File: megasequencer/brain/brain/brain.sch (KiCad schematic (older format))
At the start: 6 parts

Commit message: Add more jacks to the schema
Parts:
- added D1, D2, D? (x2): D_Schottky, symbol Device:D_Schottky
- added D3, D5: D, symbol Device:D
- added J2: EXT_CLOCK_IN, Connector_Audio:Jack_3.5mm_QingPu_WQP-PJ398SM_Vertical_CircularHoles, symbol Connector:AudioJack2_SwitchT
- added J4: ZERO_IN, Connector_Audio:Jack_3.5mm_QingPu_WQP-PJ398SM_Vertical_CircularHoles, symbol Connector:AudioJack2_SwitchT
- added J5: EXT_RATE_CV, Connector_Audio:Jack_3.5mm_QingPu_WQP-PJ398SM_Vertical_CircularHoles, symbol Connector:AudioJack2_SwitchT
- added J?: EXT_POS_CV, Connector_Audio:Jack_3.5mm_QingPu_WQP-PJ398SM_Vertical_CircularHoles, symbol Connector:AudioJack2_SwitchT
- added J?: DIR_IN, Connector_Audio:Jack_3.5mm_QingPu_WQP-PJ398SM_Vertical_CircularHoles, symbol Connector:AudioJack2_SwitchT
- added R1, R?: 1K, Resistor_THT:R_Axial_DIN0207_L6.3mm_D2.5mm_P7.62mm_Horizontal, symbol Device:R
- added R2, R3, R4, R5, R6, R? (x5): 100K, Resistor_THT:R_Axial_DIN0207_L6.3mm_D2.5mm_P7.62mm_Horizontal, symbol Device:R
- added R7, R9, R? (x2): 10K, Resistor_THT:R_Axial_DIN0207_L6.3mm_D2.5mm_P7.62mm_Horizontal, symbol Device:R
- added R?: 91K, Resistor_THT:R_Axial_DIN0207_L6.3mm_D2.5mm_P7.62mm_Horizontal, symbol Device:R
- added R?: 51K, Resistor_THT:R_Axial_DIN0207_L6.3mm_D2.5mm_P7.62mm_Horizontal, symbol Device:R
- added R?: 36K, Resistor_THT:R_Axial_DIN0207_L6.3mm_D2.5mm_P7.62mm_Horizontal, symbol Device:R
- added R?: 27K, Resistor_THT:R_Axial_DIN0207_L6.3mm_D2.5mm_P7.62mm_Horizontal, symbol Device:R
- added R?: 20K, Resistor_THT:R_Axial_DIN0207_L6.3mm_D2.5mm_P7.62mm_Horizontal, symbol Device:R
- added R?: 15K, Resistor_THT:R_Axial_DIN0207_L6.3mm_D2.5mm_P7.62mm_Horizontal, symbol Device:R
- added R?: 12K, Resistor_THT:R_Axial_DIN0207_L6.3mm_D2.5mm_P7.62mm_Horizontal, symbol Device:R
- added R?: 9K1, Resistor_THT:R_Axial_DIN0207_L6.3mm_D2.5mm_P7.62mm_Horizontal, symbol Device:R
- added R?: 7K5, Resistor_THT:R_Axial_DIN0207_L6.3mm_D2.5mm_P7.62mm_Horizontal, symbol Device:R
- added R?: 5K6, Resistor_THT:R_Axial_DIN0207_L6.3mm_D2.5mm_P7.62mm_Horizontal, symbol Device:R
- added R?: 4K3, Resistor_THT:R_Axial_DIN0207_L6.3mm_D2.5mm_P7.62mm_Horizontal, symbol Device:R
- added R?: 3K1, Resistor_THT:R_Axial_DIN0207_L6.3mm_D2.5mm_P7.62mm_Horizontal, symbol Device:R
- added R?: 2K2, Resistor_THT:R_Axial_DIN0207_L6.3mm_D2.5mm_P7.62mm_Horizontal, symbol Device:R
- added R?: 1K5, Resistor_THT:R_Axial_DIN0207_L6.3mm_D2.5mm_P7.62mm_Horizontal, symbol Device:R
- added R?: 620, Resistor_THT:R_Axial_DIN0207_L6.3mm_D2.5mm_P7.62mm_Horizontal, symbol Device:R
- added RV1: RATE_IN_OFFSET, symbol Device:R_POT
- added RV2, RV?: RATE_IN_ATT, symbol Device:R_POT
- added RV?: EXT_POS_IN_OFFSET, symbol Device:R_POT
- added SW1: CLOCK_SW, symbol Switch:SW_Push
- added SW?: POS_0_SW, symbol Switch:SW_Push
- added SW?: POS_1_SW, symbol Switch:SW_Push
- added SW?: POS_2_SW, symbol Switch:SW_Push
- added SW?: POS_3_SW, symbol Switch:SW_Push
- added SW?: POS_4_SW, symbol Switch:SW_Push
- added SW?: POS_5_SW, symbol Switch:SW_Push
- added SW?: POS_6_SW, symbol Switch:SW_Push
- added SW?: POS_7_SW, symbol Switch:SW_Push
- added SW?: POS_8_SW, symbol Switch:SW_Push
- added SW?: POS_9_SW, symbol Switch:SW_Push
- added SW?: POS_10_SW, symbol Switch:SW_Push
- added SW?: POS_11_SW, symbol Switch:SW_Push
- added SW?: POS_12_SW, symbol Switch:SW_Push
- added SW?: POS_13_SW, symbol Switch:SW_Push
- added SW?: POS_14_SW, symbol Switch:SW_Push
- added SW?: POS_15_SW, symbol Switch:SW_Push
- added U2, U? (x2): TL074, symbol Amplifier_Operational:TL074
- SW2: renamed from SW?; symbol Switch:SW_SPDT -> Switch:SW_SPDT_MSM
- gave numbers to parts that had none: 5
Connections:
- net labels added: EXT_POS, INT_CLOCK, INT_POS, RATE, SEQ_CLOCK
- wire segments 54 -> 240
- no-connect marks 0 -> 4
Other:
- moved on the sheet: D4, J3, R8

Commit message: Add int clock out
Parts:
- added D10, D9: D, symbol Device:D
- added D8: LED_INT_CLOCK, symbol Device:LED
- added J6: INT_CLOCK_OUT, Connector_Audio:Jack_3.5mm_QingPu_WQP-PJ398SM_Vertical_CircularHoles, symbol Connector:AudioJack2_SwitchT
- added R28: 1K, Resistor_THT:R_Axial_DIN0207_L6.3mm_D2.5mm_P7.62mm_Horizontal, symbol Device:R
- added SW19: SW_SPDT, symbol Switch:SW_SPDT
- gave numbers to parts that had none: 46
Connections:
- net labels added: SEQ_DIR
- wire segments 240 -> 252
- no-connect marks 4 -> 6

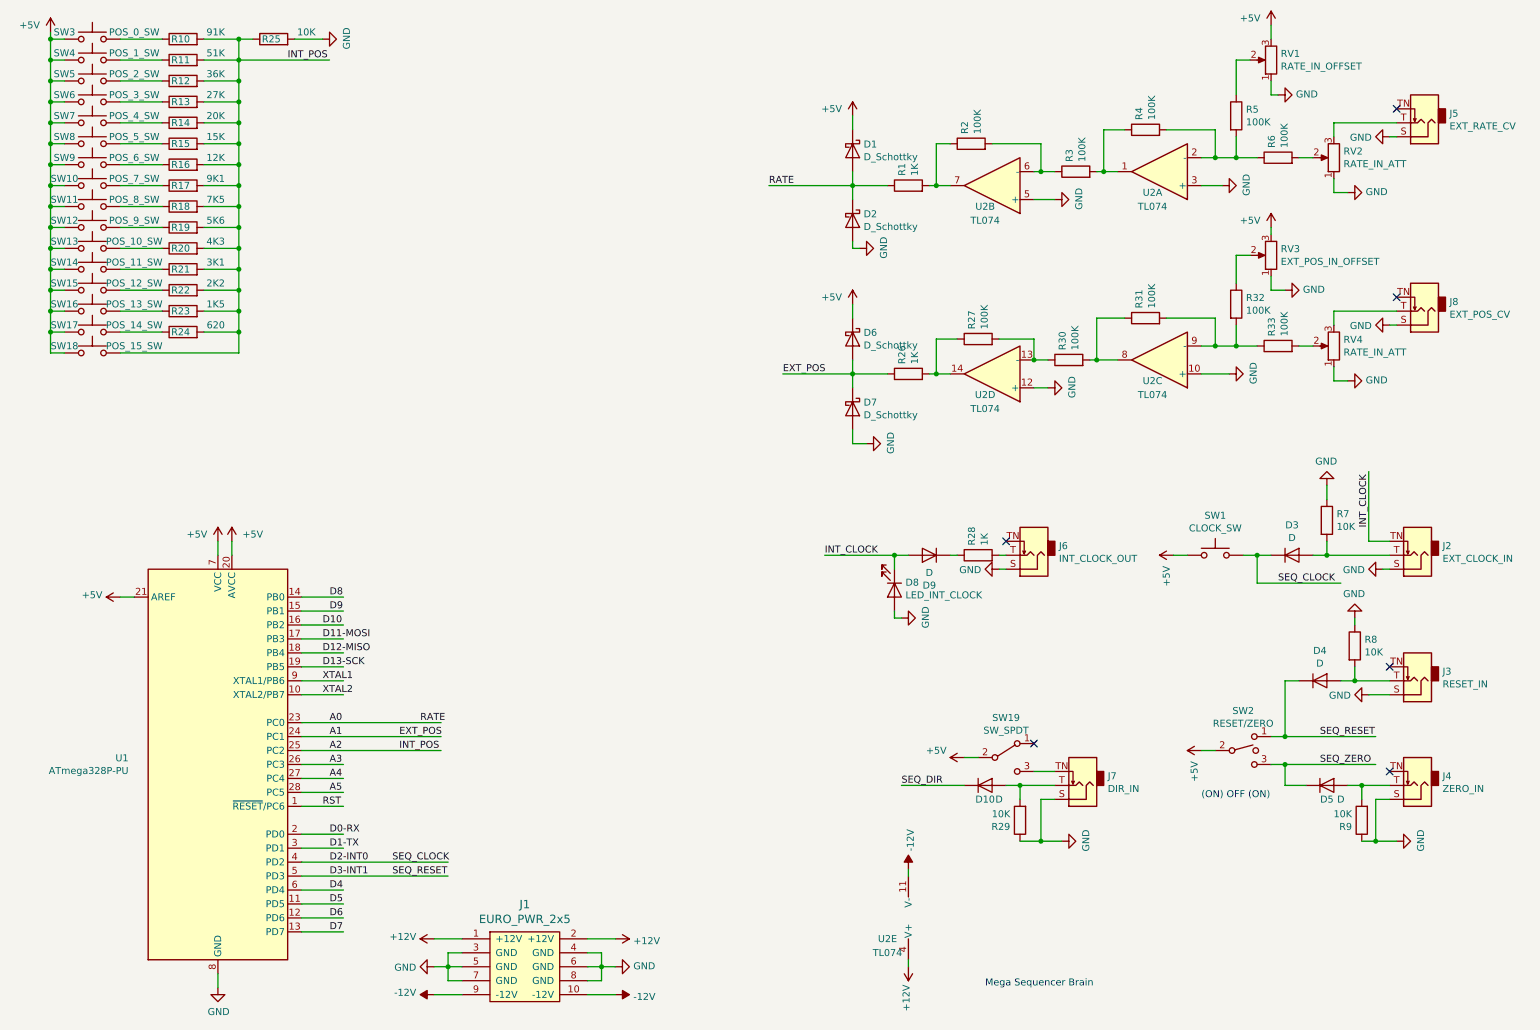
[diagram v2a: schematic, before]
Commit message: Split up into sub schemas and add layout sketch
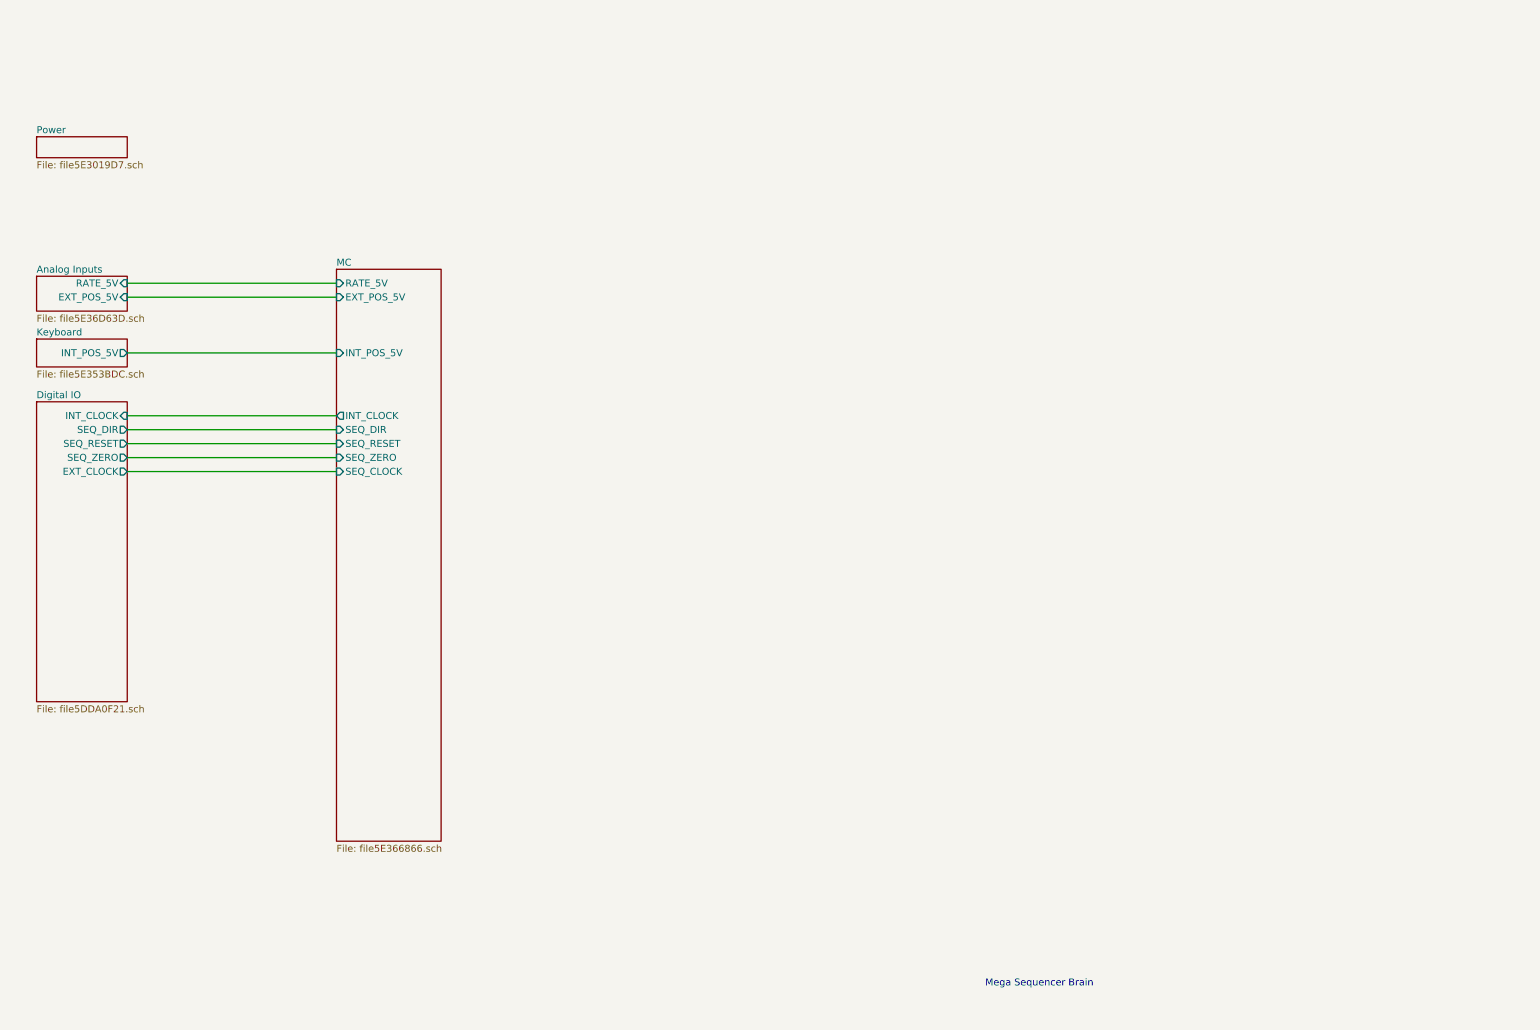
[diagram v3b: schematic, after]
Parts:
- removed D1, D2, D6, D7: D_Schottky, symbol Device:D_Schottky
- removed D10, D3, D4, D5, D9: D, symbol Device:D
- removed D8: LED_INT_CLOCK, symbol Device:LED
- removed J1: EURO_PWR_2x5, symbol eurocad:EURO_PWR_2x5
- removed J2: EXT_CLOCK_IN, Connector_Audio:Jack_3.5mm_QingPu_WQP-PJ398SM_Vertical_CircularHoles, symbol Connector:AudioJack2_SwitchT
- removed J3: RESET_IN, Connector_Audio:Jack_3.5mm_QingPu_WQP-PJ398SM_Vertical_CircularHoles, symbol Connector:AudioJack2_SwitchT
- removed J4: ZERO_IN, Connector_Audio:Jack_3.5mm_QingPu_WQP-PJ398SM_Vertical_CircularHoles, symbol Connector:AudioJack2_SwitchT
- removed J5: EXT_RATE_CV, Connector_Audio:Jack_3.5mm_QingPu_WQP-PJ398SM_Vertical_CircularHoles, symbol Connector:AudioJack2_SwitchT
- removed J6: INT_CLOCK_OUT, Connector_Audio:Jack_3.5mm_QingPu_WQP-PJ398SM_Vertical_CircularHoles, symbol Connector:AudioJack2_SwitchT
- removed J7: DIR_IN, Connector_Audio:Jack_3.5mm_QingPu_WQP-PJ398SM_Vertical_CircularHoles, symbol Connector:AudioJack2_SwitchT
- removed J8: EXT_POS_CV, Connector_Audio:Jack_3.5mm_QingPu_WQP-PJ398SM_Vertical_CircularHoles, symbol Connector:AudioJack2_SwitchT
- removed R1, R26, R28: 1K, Resistor_THT:R_Axial_DIN0207_L6.3mm_D2.5mm_P7.62mm_Horizontal, symbol Device:R
- removed R10: 91K, Resistor_THT:R_Axial_DIN0207_L6.3mm_D2.5mm_P7.62mm_Horizontal, symbol Device:R
- removed R11: 51K, Resistor_THT:R_Axial_DIN0207_L6.3mm_D2.5mm_P7.62mm_Horizontal, symbol Device:R
- removed R12: 36K, Resistor_THT:R_Axial_DIN0207_L6.3mm_D2.5mm_P7.62mm_Horizontal, symbol Device:R
- removed R13: 27K, Resistor_THT:R_Axial_DIN0207_L6.3mm_D2.5mm_P7.62mm_Horizontal, symbol Device:R
- removed R14: 20K, Resistor_THT:R_Axial_DIN0207_L6.3mm_D2.5mm_P7.62mm_Horizontal, symbol Device:R
- removed R15: 15K, Resistor_THT:R_Axial_DIN0207_L6.3mm_D2.5mm_P7.62mm_Horizontal, symbol Device:R
- removed R16: 12K, Resistor_THT:R_Axial_DIN0207_L6.3mm_D2.5mm_P7.62mm_Horizontal, symbol Device:R
- removed R17: 9K1, Resistor_THT:R_Axial_DIN0207_L6.3mm_D2.5mm_P7.62mm_Horizontal, symbol Device:R
- removed R18: 7K5, Resistor_THT:R_Axial_DIN0207_L6.3mm_D2.5mm_P7.62mm_Horizontal, symbol Device:R
- removed R19: 5K6, Resistor_THT:R_Axial_DIN0207_L6.3mm_D2.5mm_P7.62mm_Horizontal, symbol Device:R
- removed R2, R27, R3, R30, R31, R32, R33, R4, R5, R6: 100K, Resistor_THT:R_Axial_DIN0207_L6.3mm_D2.5mm_P7.62mm_Horizontal, symbol Device:R
- removed R20: 4K3, Resistor_THT:R_Axial_DIN0207_L6.3mm_D2.5mm_P7.62mm_Horizontal, symbol Device:R
- removed R21: 3K1, Resistor_THT:R_Axial_DIN0207_L6.3mm_D2.5mm_P7.62mm_Horizontal, symbol Device:R
- removed R22: 2K2, Resistor_THT:R_Axial_DIN0207_L6.3mm_D2.5mm_P7.62mm_Horizontal, symbol Device:R
- removed R23: 1K5, Resistor_THT:R_Axial_DIN0207_L6.3mm_D2.5mm_P7.62mm_Horizontal, symbol Device:R
- removed R24: 620, Resistor_THT:R_Axial_DIN0207_L6.3mm_D2.5mm_P7.62mm_Horizontal, symbol Device:R
- removed R25, R29, R7, R8, R9: 10K, Resistor_THT:R_Axial_DIN0207_L6.3mm_D2.5mm_P7.62mm_Horizontal, symbol Device:R
- removed RV1: RATE_IN_OFFSET, symbol Device:R_POT
- removed RV2, RV4: RATE_IN_ATT, symbol Device:R_POT
- removed RV3: EXT_POS_IN_OFFSET, symbol Device:R_POT
- removed SW1: CLOCK_SW, symbol Switch:SW_Push
- removed SW10: POS_7_SW, symbol Switch:SW_Push
- removed SW11: POS_8_SW, symbol Switch:SW_Push
- removed SW12: POS_9_SW, symbol Switch:SW_Push
- removed SW13: POS_10_SW, symbol Switch:SW_Push
- removed SW14: POS_11_SW, symbol Switch:SW_Push
- removed SW15: POS_12_SW, symbol Switch:SW_Push
- removed SW16: POS_13_SW, symbol Switch:SW_Push
- removed SW17: POS_14_SW, symbol Switch:SW_Push
- removed SW18: POS_15_SW, symbol Switch:SW_Push
- removed SW19: SW_SPDT, symbol Switch:SW_SPDT
- removed SW2: RESET/ZERO, symbol Switch:SW_SPDT_MSM
- removed SW3: POS_0_SW, symbol Switch:SW_Push
- removed SW4: POS_1_SW, symbol Switch:SW_Push
- removed SW5: POS_2_SW, symbol Switch:SW_Push
- removed SW6: POS_3_SW, symbol Switch:SW_Push
- removed SW7: POS_4_SW, symbol Switch:SW_Push
- removed SW8: POS_5_SW, symbol Switch:SW_Push
- removed SW9: POS_6_SW, symbol Switch:SW_Push
- removed U1: ATmega328P-PU, Package_DIP:DIP-28_W7.62mm, symbol MCU_Microchip_ATmega:ATmega328P-PU
- removed U2: TL074, symbol Amplifier_Operational:TL074
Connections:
- net labels removed: +12V, +5V, -12V, A0, A1, A2, A3, A4, A5, D0-RX, D1-TX, D10, D11-MOSI, D12-MISO, D13-SCK, D2-INT0, D3-INT1, D4, D5, D6, D7, D8, D9, EXT_POS, GND, INT_CLOCK, INT_POS, RATE, RST, SEQ_CLOCK, SEQ_DIR, SEQ_RESET, SEQ_ZERO, XTAL1, XTAL2
- wire segments 252 -> 8
- no-connect marks 6 -> 0
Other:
- note removed: "(ON) OFF (ON)"

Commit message: Add pwr, more inputs and outputs
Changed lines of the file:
@@
 $Descr A4 11693 8268
 encoding utf-8
-Sheet 1 6
+Sheet 1 7
 Title ""
 Date ""
@@
 $EndSheet
 $Sheet
-S 600  2850 650  200
+S 600  3000 650  200
 U 5E353BDD
 F0 "Keyboard" 50
 F1 "file5E353BDC.sch" 50
-F2 "INT_POS_5V" O R 1250 2950 50
+F2 "INT_POS_5V" O R 1250 3100 50
 $EndSheet
 $Sheet
@@
 F2 "RATE_5V" I L 2750 2450 50
 F3 "EXT_POS_5V" I L 2750 2550 50
-F4 "INT_POS_5V" I L 2750 2950 50
-F5 "SEQ_CLOCK" I L 2750 3800 50
-F6 "SEQ_RESET" I L 2750 3600 50
-F7 "SEQ_DIR" I L 2750 3500 50
-F8 "INT_CLOCK" O L 2750 3400 50
-F9 "SEQ_ZERO" I L 2750 3700 50
+F4 "INT_POS_5V" I L 2750 3100 50
+F5 "SEQ_CLOCK" I L 2750 3950 50
+F6 "SEQ_RESET" I L 2750 3750 50
+F7 "SEQ_DIR" I L 2750 3650 50
+F8 "INT_CLOCK" O L 2750 3550 50
+F9 "SEQ_ZERO" I L 2750 3850 50
+F10 "PULSE_LENGTH_5V" I L 2750 2650 50
 $EndSheet
 $Sheet
-S 600  2400 650  250
+S 600  2400 650  450
 U 5E36D63E
 F0 "Analog Inputs" 50
 F1 "file5E36D63D.sch" 50
 F2 "RATE_5V" I R 1250 2450 50
-F3 "EXT_POS_5V" I R 1250 2550 50
+F3 "POS_5V" O R 1250 2550 50
+F4 "PULSE_LENGTH_5V" O R 1250 2650 50
 $EndSheet
 Wire Wire Line
@@
 	1250 2550 2750 2550
 Wire Wire Line
-	1250 2950 2750 2950
+	1250 3100 2750 3100
 $Sheet
-S 600  3300 650  2150
+S 600  3450 650  1000
 U 5DDA0F22
 F0 "Digital IO" 50
 F1 "file5DDA0F21.sch" 50
-F2 "INT_CLOCK" I R 1250 3400 50
-F3 "SEQ_DIR" O R 1250 3500 50
-F4 "SEQ_RESET" O R 1250 3600 50
-F5 "SEQ_ZERO" O R 1250 3700 50
-F6 "EXT_CLOCK" O R 1250 3800 50
+F2 "INT_CLOCK" I R 1250 3550 50
+F3 "SEQ_DIR" O R 1250 3650 50
+F4 "SEQ_RESET" O R 1250 3750 50
+F5 "SEQ_ZERO" O R 1250 3850 50
+F6 "EXT_CLOCK" O R 1250 3950 50
+F7 "STEP_PULSE" I R 1250 4050 50
 $EndSheet
 Wire Wire Line
-	1250 3500 2750 3500
+	1250 3650 2750 3650
 Wire Wire Line
-	1250 3600 2750 3600
+	1250 3750 2750 3750
 Wire Wire Line
-	1250 3800 2750 3800
+	1250 3950 2750 3950
 Wire Wire Line
-	1250 3400 2750 3400
+	1250 3550 2750 3550
 Wire Wire Line
-	1250 3700 2750 3700
+	1250 3850 2750 3850
+Wire Wire Line
+	1250 2650 2750 2650
+$Sheet
+S 600  4700 650  900
+U 5DDEBCF4
+F0 "OUTPUTS" 50
+F1 "file5DDEBCF3.sch" 50
+$EndSheet
 $EndSCHEMATC
